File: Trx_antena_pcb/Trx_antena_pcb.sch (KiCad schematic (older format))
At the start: 5 parts, among them P1 CONN_5, P2 CONN_4

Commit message: "Segundas correcciones. Documentacion"
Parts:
- removed P1: CONN_5, Poncho_Modelos:bornier5, symbol CONN_5
- removed P2: CONN_4, Poncho_Modelos:bornier4, symbol CONN_4
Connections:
- net labels removed: VREG_EN
- wire segments 22 -> 9
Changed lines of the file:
@@
 EESchema Schematic File Version 2
-LIBS:dongle
-LIBS:ubertooth-symbols
-LIBS:Ej2-cache
-LIBS:juanvmont-cache
 LIBS:device
 LIBS:Trx_antena_pcb-cache
@@
 $Descr A4 11693 8268
 encoding utf-8
-Sheet 1 3
-Title "Poncho Izquierdo - Modelo - Ejemplo - Template"
-Date "2015-10-06"
+Sheet 1 2
+Title "Poncho EDU-CIAA-NXP RF 2.4GHz Antena PCB"
+Date "2016-12-02"
 Rev "1.0"
 Comp "Proyecto CIAA - COMPUTADORA INDUSTRIAL ABIERTA ARGENTINA"
 Comment1 "https://github.com/ciaa/Ponchos/tree/master/modelos/doc"
-Comment2 "Autores y Licencia del template (Diego Brengi - UNLaM)"
-Comment3 "Autor del poncho (COMPLETAR NOMBRE Y APELLIDO). Ver directorio \"doc\""
-Comment4 "CÓDIGO PONCHO: "
+Comment2 "Basado en el template de Diego Brengi - UNLaM"
+Comment3 "Autor y Licencia del poncho (Juan Vicente Montilla-FIUBA). Ver directorio \"doc\""
+Comment4 "https://github.com/Juanvmont/Poncho-EDU-CIAA-NXP-RF-2.4GHz-Antena-PCB.git"
 $EndDescr
 $Comp
@@
 	-1   0    0    -1
 $EndComp
-$Comp
-L CONN_5 P1
-U 1 1 560ED139
-P 5100 4200
-F 0 "P1" V 5050 4200 50  0000 C CNN
-F 1 "CONN_5" V 5150 4200 50  0000 C CNN
-F 2 "Poncho_Modelos:bornier5" H 5550 4600 60  0000 C CNN
-F 3 "" H 5100 4200 60  0000 C CNN
-	1    5100 4200
-	1    0    0    1
-$EndComp
-$Comp
-L CONN_4 P2
-U 1 1 560ED17A
-P 3300 5950
-F 0 "P2" V 3250 5950 50  0000 C CNN
-F 1 "CONN_4" V 3350 5950 50  0000 C CNN
-F 2 "Poncho_Modelos:bornier4" H 3700 5650 60  0000 C CNN
-F 3 "" H 3300 5950 60  0000 C CNN
-	1    3300 5950
-	-1   0    0    1
-$EndComp
 Wire Wire Line
 	4500 4200 4750 4200
 Wire Wire Line
 	4750 4300 4500 4300
-Wire Wire Line
-	4750 4000 4600 4000
-Wire Wire Line
-	4600 4000 4600 3900
-Wire Wire Line
-	4750 4400 4650 4400
-Wire Wire Line
-	4650 4400 4650 4500
-$Comp
-L GND #PWR4
-U 1 1 560ED8F9
-P 4650 4500
-F 0 "#PWR4" H 4650 4500 30  0001 C CNN
-F 1 "GND" H 4650 4430 30  0001 C CNN
-F 2 "" H 4650 4500 60  0000 C CNN
-F 3 "" H 4650 4500 60  0000 C CNN
-	1    4650 4500
-	1    0    0    -1
-$EndComp
-$Comp
-L GND #PWR1
-U 1 1 560ED917
-P 3750 6250
-F 0 "#PWR1" H 3750 6250 30  0001 C CNN
-F 1 "GND" H 3750 6180 30  0001 C CNN
-F 2 "" H 3750 6250 60  0000 C CNN
-F 3 "" H 3750 6250 60  0000 C CNN
-	1    3750 6250
-	-1   0    0    -1
-$EndComp
-Wire Wire Line
-	3650 6100 3750 6100
-Wire Wire Line
-	3750 6100 3750 6250
 NoConn ~ 4150 6100
 NoConn ~ 4150 6300
@@
 	1    0    0    -1
 $EndComp
-$Comp
-L +5VP #PWR3
-U 1 1 5613257D
-P 4600 3900
-F 0 "#PWR3" H 4600 3990 20  0001 C CNN
-F 1 "+5VP" H 4600 3990 30  0000 C CNN
-F 2 "" H 4600 3900 60  0000 C CNN
-F 3 "" H 4600 3900 60  0000 C CNN
-	1    4600 3900
-	1    0    0    -1
-$EndComp
 Wire Wire Line
 	5800 2000 5800 1950
@@
 NoConn ~ 4200 2300
 NoConn ~ 4200 2200
-Wire Wire Line
-	4150 6200 3900 6200
-Wire Wire Line
-	3900 6200 3900 6000
-Wire Wire Line
-	3900 6000 3650 6000
-Wire Wire Line
-	4150 6000 3950 6000
-Wire Wire Line
-	3950 6000 3950 5900
-Wire Wire Line
-	3950 5900 3650 5900
-Wire Wire Line
-	4150 5800 3650 5800
 $Comp
 L PCB_HOLE H2
@@
 Agujeros para visualización de LEDs
 $Sheet
-S 500  950  1150 1550
-U 582F7A78
-F0 "Conectores" 60
-F1 "Conectores.sch" 60
-$EndSheet
-$Sheet
-S 800  3200 800  2750
+S 800  2400 800  2750
 U 582F8126
 F0 "Radio" 60
 F1 "Radio.sch" 60
+F2 "SO" O R 1600 2700 60
+F3 "SI" I R 1600 2800 60
+F4 "VREG_EN" I R 1600 2600 60
+F5 "SCLK" I R 1600 2900 60
+F6 "GPIO5" B R 1600 3000 60
+F7 "GPIO4" B R 1600 3100 60
+F8 "GPIO3" B R 1600 3200 60
+F9 "GPIO2" B R 1600 3300 60
+F10 "GPIO1" B R 1600 3400 60
+F11 "GPIO0" B R 1600 3500 60
+F12 "RST" I R 1600 3600 60
 $EndSheet
-Text HLabel 1600 3250 0    60   Input ~ 0
-VREG_EN
 $EndSCHEMATC

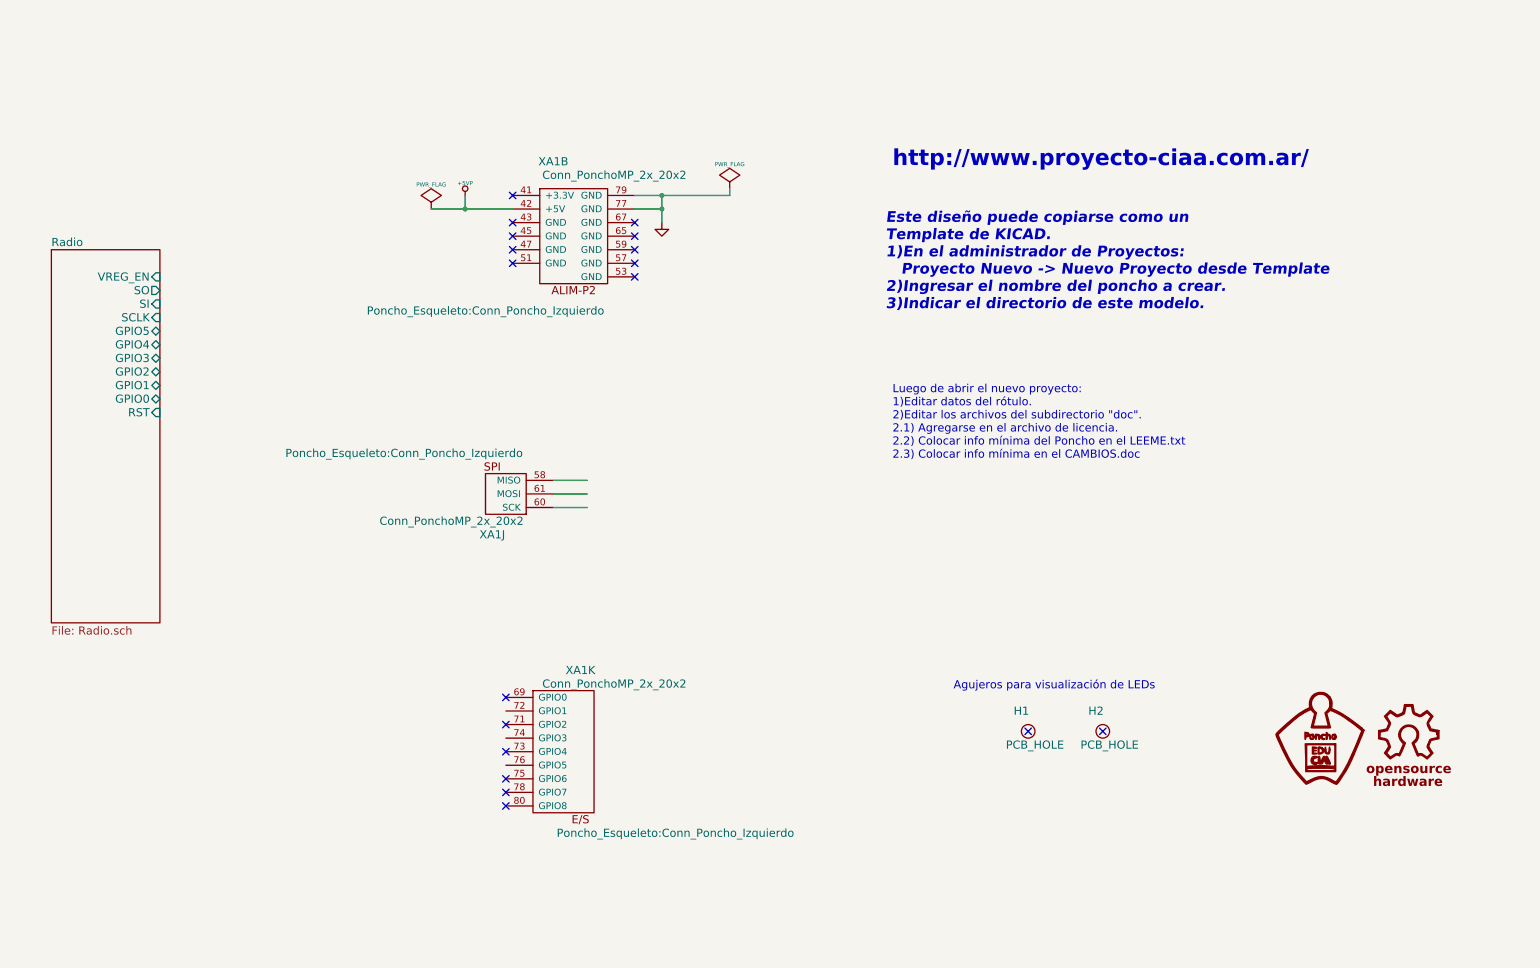
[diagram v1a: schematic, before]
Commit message: Completando esquematico de RF
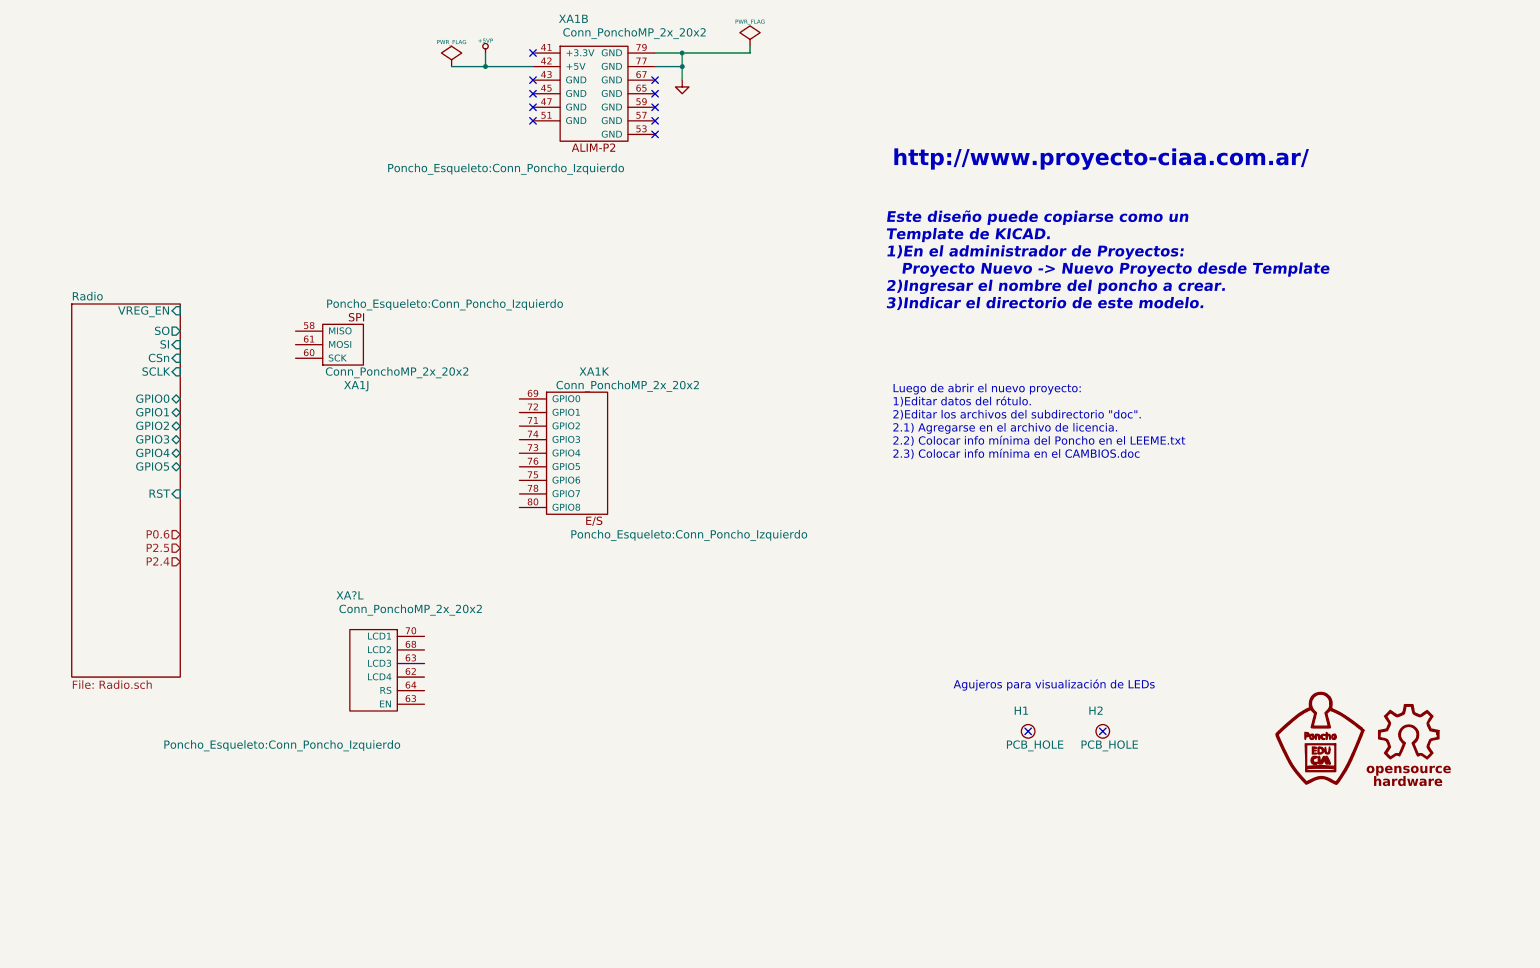
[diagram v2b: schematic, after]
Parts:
- added XA?: Conn_PonchoMP_2x_20x2, Poncho_Esqueleto:Conn_Poncho_Izquierdo, symbol Conn_PonchoMP_2x_20x2
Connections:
- net labels added: P0.6, P2.4, P2.5
- wire segments 9 -> 6
- no-connect marks 18 -> 12
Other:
- moved on the sheet: XA1B, XA1J, XA1K
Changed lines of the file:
@@
 L Conn_PonchoMP_2x_20x2 XA1
 U 11 1 560E5596
-P 4600 6000
-F 0 "XA1" H 4500 6500 60  0000 C CNN
-F 1 "Conn_PonchoMP_2x_20x2" H 4250 6400 60  0000 C CNN
-F 2 "Poncho_Esqueleto:Conn_Poncho_Izquierdo" H 3800 5300 60  0000 C CNN
-F 3 "" H 4450 6350 60  0000 C CNN
-	11   4600 6000
+P 4700 3800
+F 0 "XA1" H 4600 4300 60  0000 C CNN
+F 1 "Conn_PonchoMP_2x_20x2" H 4350 4200 60  0000 C CNN
+F 2 "Poncho_Esqueleto:Conn_Poncho_Izquierdo" H 3900 3100 60  0000 C CNN
+F 3 "" H 4550 4150 60  0000 C CNN
+	11   4700 3800
 	-1   0    0    -1
 $EndComp
-Wire Wire Line
-	4500 4200 4750 4200
-Wire Wire Line
-	4750 4300 4500 4300
-NoConn ~ 4150 6100
-NoConn ~ 4150 6300
-NoConn ~ 4150 6400
-NoConn ~ 4150 6500
-NoConn ~ 4150 5700
-NoConn ~ 4150 5900
 Text Notes 7000 3950 0    60   ~ 0
 Luego de abrir el nuevo proyecto:\n1)Editar datos del rótulo.\n2)Editar los archivos del subdirectorio "doc".\n2.1) Agregarse en el archivo de licencia.\n2.2) Colocar info mínima del Poncho en el LEEME.txt\n2.3) Colocar info mínima en el CAMBIOS.doc
@@
 L Conn_PonchoMP_2x_20x2 XA1
 U 10 1 560E54EF
-P 4150 4200
-F 0 "XA1" H 4050 4500 60  0000 C CNN
-F 1 "Conn_PonchoMP_2x_20x2" H 3750 4400 60  0000 C CNN
-F 2 "Poncho_Esqueleto:Conn_Poncho_Izquierdo" H 3400 3900 60  0000 C CNN
-F 3 "" H 4000 4550 60  0000 C CNN
-	10   4150 4200
-	1    0    0    1
+P 2950 3100
+F 0 "XA1" H 2850 3400 60  0000 C CNN
+F 1 "Conn_PonchoMP_2x_20x2" H 2550 3300 60  0000 C CNN
+F 2 "Poncho_Esqueleto:Conn_Poncho_Izquierdo" H 2200 2800 60  0000 C CNN
+F 3 "" H 2800 3450 60  0000 C CNN
+	10   2950 3100
+	-1   0    0    1
 $EndComp
-Wire Wire Line
-	4750 4100 4500 4100
-Connection ~ 3850 2100
 $Comp
 L PWR_FLAG #FLG1
 U 1 1 560EE826
-P 3600 2100
-F 0 "#FLG1" H 3600 2195 30  0001 C CNN
-F 1 "PWR_FLAG" H 3600 2280 30  0000 C CNN
-F 2 "" H 3600 2100 60  0000 C CNN
-F 3 "" H 3600 2100 60  0000 C CNN
-	1    3600 2100
+P 3750 1050
+F 0 "#FLG1" H 3750 1145 30  0001 C CNN
+F 1 "PWR_FLAG" H 3750 1230 30  0000 C CNN
+F 2 "" H 3750 1050 60  0000 C CNN
+F 3 "" H 3750 1050 60  0000 C CNN
+	1    3750 1050
 	1    0    0    -1
 $EndComp
-Wire Wire Line
-	3850 2100 3850 2000
-Wire Wire Line
-	3600 2100 4200 2100
 $Comp
 L +5VP #PWR2
 U 1 1 560EE7D3
-P 3850 2000
-F 0 "#PWR2" H 3850 2090 20  0001 C CNN
-F 1 "+5VP" H 3850 2090 30  0000 C CNN
-F 2 "" H 3850 2000 60  0000 C CNN
-F 3 "" H 3850 2000 60  0000 C CNN
-	1    3850 2000
+P 4000 950
+F 0 "#PWR2" H 4000 1040 20  0001 C CNN
+F 1 "+5VP" H 4000 1040 30  0000 C CNN
+F 2 "" H 4000 950 60  0000 C CNN
+F 3 "" H 4000 950 60  0000 C CNN
+	1    4000 950
 	1    0    0    -1
 $EndComp
-Connection ~ 5300 2100
-Wire Wire Line
-	5100 2000 5800 2000
-Wire Wire Line
-	5300 2000 5300 2200
-Wire Wire Line
-	5100 2100 5300 2100
 $Comp
 L GND #PWR5
 U 1 1 560EE345
-P 5300 2200
-F 0 "#PWR5" H 5300 2200 30  0001 C CNN
-F 1 "GND" H 5300 2130 30  0001 C CNN
-F 2 "" H 5300 2200 60  0000 C CNN
-F 3 "" H 5300 2200 60  0000 C CNN
-	1    5300 2200
+P 5450 1150
+F 0 "#PWR5" H 5450 1150 30  0001 C CNN
+F 1 "GND" H 5450 1080 30  0001 C CNN
+F 2 "" H 5450 1150 60  0000 C CNN
+F 3 "" H 5450 1150 60  0000 C CNN
+	1    5450 1150
 	1    0    0    -1
 $EndComp
-NoConn ~ 5100 2200
-NoConn ~ 5100 2300
-NoConn ~ 5100 2400
-NoConn ~ 5100 2500
-NoConn ~ 5100 2600
-NoConn ~ 4200 2500
-NoConn ~ 4200 2000
+NoConn ~ 5250 1150
+NoConn ~ 5250 1250
+NoConn ~ 5250 1350
+NoConn ~ 5250 1450
+NoConn ~ 5250 1550
+NoConn ~ 4350 1450
+NoConn ~ 4350 950
 $Comp
 L Conn_PonchoMP_2x_20x2 XA1
 U 2 1 560EE110
-P 4650 2300
-F 0 "XA1" H 4500 2850 60  0000 C CNN
-F 1 "Conn_PonchoMP_2x_20x2" H 4950 2750 60  0000 C CNN
-F 2 "Poncho_Esqueleto:Conn_Poncho_Izquierdo" H 4000 1750 60  0000 C CNN
-F 3 "" H 4500 2650 60  0000 C CNN
-	2    4650 2300
+P 4800 1250
+F 0 "XA1" H 4650 1800 60  0000 C CNN
+F 1 "Conn_PonchoMP_2x_20x2" H 5100 1700 60  0000 C CNN
+F 2 "Poncho_Esqueleto:Conn_Poncho_Izquierdo" H 4150 700 60  0000 C CNN
+F 3 "" H 4650 1600 60  0000 C CNN
+	2    4800 1250
 	1    0    0    -1
 $EndComp
@@
 L PWR_FLAG #FLG2
 U 1 1 560EDE73
-P 5800 1950
-F 0 "#FLG2" H 5800 2045 30  0001 C CNN
-F 1 "PWR_FLAG" H 5800 2130 30  0000 C CNN
-F 2 "" H 5800 1950 60  0000 C CNN
-F 3 "" H 5800 1950 60  0000 C CNN
-	1    5800 1950
+P 5950 900
+F 0 "#FLG2" H 5950 995 30  0001 C CNN
+F 1 "PWR_FLAG" H 5950 1080 30  0000 C CNN
+F 2 "" H 5950 900 60  0000 C CNN
+F 3 "" H 5950 900 60  0000 C CNN
+	1    5950 900
 	1    0    0    -1
 $EndComp
-Wire Wire Line
-	5800 2000 5800 1950
-Connection ~ 5300 2000
-NoConn ~ 4200 2400
-NoConn ~ 4200 2300
-NoConn ~ 4200 2200
+NoConn ~ 4350 1350
+NoConn ~ 4350 1250
+NoConn ~ 4350 1150
 $Comp
 L PCB_HOLE H2
@@
 Agujeros para visualización de LEDs
 $Sheet
-S 800  2400 800  2750
+S 950  2800 800  2750
 U 582F8126
 F0 "Radio" 60
 F1 "Radio.sch" 60
-F2 "SO" O R 1600 2700 60
-F3 "SI" I R 1600 2800 60
-F4 "VREG_EN" I R 1600 2600 60
-F5 "SCLK" I R 1600 2900 60
-F6 "GPIO5" B R 1600 3000 60
-F7 "GPIO4" B R 1600 3100 60
-F8 "GPIO3" B R 1600 3200 60
-F9 "GPIO2" B R 1600 3300 60
-F10 "GPIO1" B R 1600 3400 60
-F11 "GPIO0" B R 1600 3500 60
-F12 "RST" I R 1600 3600 60
+F2 "SO" O R 1750 3000 60
+F3 "SI" I R 1750 3100 60
+F4 "VREG_EN" I R 1750 2850 60
+F5 "SCLK" I R 1750 3300 60
+F6 "GPIO0" B R 1750 3500 60
+F7 "GPIO1" B R 1750 3600 60
+F8 "GPIO2" B R 1750 3700 60
+F9 "GPIO3" B R 1750 3800 60
+F10 "GPIO4" B R 1750 3900 60
+F11 "GPIO5" B R 1750 4000 60
+F12 "RST" I R 1750 4200 60
+F13 "CSn" I R 1750 3200 60
 $EndSheet
+$Comp
+L Conn_PonchoMP_2x_20x2 XA?
+U 12 1 584DA9F1
+P 3150 5500
+F 0 "XA?" H 3000 6050 60  0000 C CNN
+F 1 "Conn_PonchoMP_2x_20x2" H 3450 5950 60  0000 C CNN
+F 2 "Poncho_Esqueleto:Conn_Poncho_Izquierdo" H 2500 4950 60  0000 C CNN
+F 3 "" H 3000 5850 60  0000 C CNN
+	12   3150 5500
+	1    0    0    -1
+$EndComp
+Text HLabel 1750 4500 0    60   Input ~ 0
+P0.6
+Text HLabel 1750 4600 0    60   Input ~ 0
+P2.5
+Text HLabel 1750 4700 0    60   Input ~ 0
+P2.4
+Connection ~ 4000 1050
+Wire Wire Line
+	4000 1050 4000 950
+Wire Wire Line
+	3750 1050 4350 1050
+Connection ~ 5450 1050
+Wire Wire Line
+	5250 950  5950 950
+Wire Wire Line
+	5450 950  5450 1150
+Wire Wire Line
+	5250 1050 5450 1050
+Wire Wire Line
+	5950 950  5950 900
+Connection ~ 5450 950
 $EndSCHEMATC

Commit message: mattching pin tou from edu ciaa to poncho
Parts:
- removed XA?: Conn_PonchoMP_2x_20x2, Poncho_Esqueleto:Conn_Poncho_Izquierdo, symbol Conn_PonchoMP_2x_20x2
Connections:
- net labels removed: P0.6, P2.4, P2.5
- wire segments 6 -> 18
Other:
- moved on the sheet: XA1B
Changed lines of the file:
@@
 L Conn_PonchoMP_2x_20x2 XA1
 U 2 1 560EE110
-P 4800 1250
-F 0 "XA1" H 4650 1800 60  0000 C CNN
-F 1 "Conn_PonchoMP_2x_20x2" H 5100 1700 60  0000 C CNN
-F 2 "Poncho_Esqueleto:Conn_Poncho_Izquierdo" H 4150 700 60  0000 C CNN
-F 3 "" H 4650 1600 60  0000 C CNN
-	2    4800 1250
+P 3250 5300
+F 0 "XA1" H 3100 5850 60  0000 C CNN
+F 1 "Conn_PonchoMP_2x_20x2" H 3550 5750 60  0000 C CNN
+F 2 "Poncho_Esqueleto:Conn_Poncho_Izquierdo" H 2600 4750 60  0000 C CNN
+F 3 "" H 3100 5650 60  0000 C CNN
+	2    3250 5300
 	1    0    0    -1
 $EndComp
@@
 F2 "SO" O R 1750 3000 60
 F3 "SI" I R 1750 3100 60
-F4 "VREG_EN" I R 1750 2850 60
-F5 "SCLK" I R 1750 3300 60
+F4 "VREG_EN" I R 1750 4950 60
+F5 "SCLK" I R 1750 3200 60
 F6 "GPIO0" B R 1750 3500 60
 F7 "GPIO1" B R 1750 3600 60
@@
 F10 "GPIO4" B R 1750 3900 60
 F11 "GPIO5" B R 1750 4000 60
-F12 "RST" I R 1750 4200 60
-F13 "CSn" I R 1750 3200 60
+F12 "RST" I R 1750 5100 60
+F13 "CSn" I R 1750 3300 60
+F14 "GPIO6" B R 1750 4100 60
+F15 "GPIO7" B R 1750 4200 60
+F16 "GPIO8" B R 1750 4300 60
 $EndSheet
-$Comp
-L Conn_PonchoMP_2x_20x2 XA?
-U 12 1 584DA9F1
-P 3150 5500
-F 0 "XA?" H 3000 6050 60  0000 C CNN
-F 1 "Conn_PonchoMP_2x_20x2" H 3450 5950 60  0000 C CNN
-F 2 "Poncho_Esqueleto:Conn_Poncho_Izquierdo" H 2500 4950 60  0000 C CNN
-F 3 "" H 3000 5850 60  0000 C CNN
-	12   3150 5500
-	1    0    0    -1
-$EndComp
-Text HLabel 1750 4500 0    60   Input ~ 0
-P0.6
-Text HLabel 1750 4600 0    60   Input ~ 0
-P2.5
-Text HLabel 1750 4700 0    60   Input ~ 0
-P2.4
 Connection ~ 4000 1050
 Wire Wire Line
@@
 	5950 950  5950 900
 Connection ~ 5450 950
+Wire Wire Line
+	2600 3000 1750 3000
+Wire Wire Line
+	2600 3100 1750 3100
+Wire Wire Line
+	2600 3200 1750 3200
+Wire Wire Line
+	1750 3500 4250 3500
+Wire Wire Line
+	4250 3600 1750 3600
+Wire Wire Line
+	1750 3700 4250 3700
+Wire Wire Line
+	1750 3800 4250 3800
+Wire Wire Line
+	1750 3900 4250 3900
+Wire Wire Line
+	1750 4000 4250 4000
+Wire Wire Line
+	1750 4100 4250 4100
+Wire Wire Line
+	1750 4200 4250 4200
+Wire Wire Line
+	1750 4300 4250 4300
 $EndSCHEMATC
